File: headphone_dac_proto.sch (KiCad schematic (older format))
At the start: 66 parts, among them J1 USB_B_Mini, J2 Bluetooth, J3 Prog, J6 Headphones, U1 LT3042xMSE, U2 CY8C5888LTI-LP097, U3 CS4344, U4 TPA6139A2, Y1 Crystal_GND24

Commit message: ..
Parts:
- Y1: value Crystal_GND24 -> 12.288MHz
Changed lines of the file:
@@
 U 1 1 5F038FE4
 P 7200 9500
-F 0 "Y1" H 7006 9454 50  0000 R CNN
-F 1 "Crystal_GND24" H 7006 9545 50  0000 R CNN
+F 0 "Y1" H 7100 9300 50  0000 R CNN
+F 1 "12.288MHz" H 7750 9350 50  0000 R CNN
 F 2 "Crystal:Crystal_SMD_Abracon_ABM3B-4Pin_5.0x3.2mm" H 7200 9500 50  0001 C CNN
 F 3 "~" H 7200 9500 50  0001 C CNN

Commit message: Change programming connector. Finish BOM
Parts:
- removed J3: Prog, conn_prog:FTSH-105, symbol Connector_Generic:Conn_02x05_Odd_Even
- added J3: Conn_01x05_Male, Connector_PinHeader_2.54mm:PinHeader_1x05_P2.54mm_Vertical, symbol Connector:Conn_01x05_Male
- C1, C2, C27, C3, C32, C33, C34, C35, C36, C4: Manufacturer (none) -> KEMET; Manufacturer Part Number (none) -> C0603C105K3RAC7411; Mouser Part Number (none) -> 80-C0603C105K3RLR
- C10, C11, C12, C13, C14, C20, C22, C5, C6, C9: Manufacturer (none) -> KEMET; Manufacturer Part Number (none) -> C0603C104K5RAC3121; Mouser Part Number (none) -> 80-C603C104K5RAC3121
- C15, C16, C17, C21: Manufacturer (none) -> KEMET; Manufacturer Part Number (none) -> C0805C475K3RACTU; Mouser Part Number (none) -> 80-C0805C475K3RACTU
- C18, C19, C7, C8: Manufacturer (none) -> KEMET; Manufacturer Part Number (none) -> C0603C150K5RAC7867; Mouser Part Number (none) -> 80-C0603C150K5RACTU
- C23: Manufacturer (none) -> KEMET; Manufacturer Part Number (none) -> C0805C106K8RACAUTO; Mouser Part Number (none) -> 80-C0805C106K8RAUTO
- C24, C25, C26, C30, C31: Manufacturer (none) -> TDK; Manufacturer Part Number (none) -> CGA4J1X7R1E335K125AC; Mouser Part Number (none) -> 810-CGA4J1X7R1E335K
- C28, C29: Manufacturer (none) -> KEMET; Manufacturer Part Number (none) -> C0603C272J5GACAUTO; Mouser Part Number (none) -> 80-C0603C272J5GAUTO
- FB1: Manufacturer (none) -> TDK; Manufacturer Part Number (none) -> KMZ1608SHR601ATD25; Mouser Part Number (none) -> 810-KMZ1608SHR601ATD
- H1, H2, H3, H4, R1: Config (none) -> dnp
- J1: Manufacturer (none) -> Wurth Elektronik; Manufacturer Part Number (none) -> 65100516121; Mouser Part Number (none) -> 710-65100516121
- J2: Manufacturer (none) -> Harwin; Manufacturer Part Number (none) -> M20-9761046; Mouser Part Number (none) -> 855-M20-9761046
- J6: Manufacturer (none) -> CUI Devices; Manufacturer Part Number (none) -> SJ1-3535NG-GR; Mouser Part Number (none) -> 490-SJ1-3535NG-GR
- R10: Manufacturer (none) -> Vishay / Dale; Manufacturer Part Number (none) -> RCS060382K0FKEA; Mouser Part Number (none) -> 71-RCS060382K0FKEA
- R2, R3: Manufacturer (none) -> Vishay / Dale; Manufacturer Part Number (none) -> CRCW060327R0FKEAC; Mouser Part Number (none) -> 71-CRCW060327R0FKEAC
- R4: Manufacturer (none) -> Panasonic; Manufacturer Part Number (none) -> ERJ-UP3D1001V; Mouser Part Number (none) -> 667-ERJ-UP3D1001V
- R5: Manufacturer (none) -> Panasonic; Manufacturer Part Number (none) -> ERJ-PB3B3322V; Mouser Part Number (none) -> 667-ERJ-PB3B3322V
- R6, R7: Manufacturer (none) -> Panasonic; Manufacturer Part Number (none) -> ERJ-UP3F1002V; Mouser Part Number (none) -> 667-ERJ-UP3F1002V
- R8, R9: Manufacturer (none) -> Panasonic; Manufacturer Part Number (none) -> ERJ-UP3F4700V; Mouser Part Number (none) -> 667-ERJ-UP3F4700V
- RV1: Manufacturer (none) -> Bourns; Manufacturer Part Number (none) -> PTV09A-4025U-A104; Mouser Part Number (none) -> 652-PTV09A-4025UA104
- RV2, RV3: Manufacturer (none) -> Bourns; Manufacturer Part Number (none) -> PTV09A-4025F-B104; Mouser Part Number (none) -> 652-PTV09A4025FB104
- SW1, SW2, SW3: Manufacturer (none) -> ALPS; Manufacturer Part Number (none) -> SKHHDUA010; Mouser Part Number (none) -> 688-SKHHDU
- U1: Manufacturer (none) -> Analog Devices; Manufacturer Part Number (none) -> LT3042EMSE#PBF; Mouser Part Number (none) -> 584-LT3042EMSE#PBF
- U2: Mouser Part Number (none) -> 727-CY8C5888LTILP097
- U3: Manufacturer (none) -> Cirrus Logic; Manufacturer Part Number (none) -> CS4344-CZZR; Mouser Part Number (none) -> 777-CS4344-CZZR
- U4: Manufacturer (none) -> Texas Instruments; Manufacturer Part Number (none) -> TPA6139A2PWR; Mouser Part Number (none) -> 595-TPA6139A2PWR
- Y1: Manufacturer (none) -> ABRACON; Manufacturer Part Number (none) -> ABM3B-12.288MHZ-10-1-U-T; Mouser Part Number (none) -> 815-ABM3B-12.288-T
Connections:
- net labels added: swdck, swdio
- net labels removed: tck, tdi, tdo, tms
- wire segments 261 -> 250
- no-connect marks 48 -> 50

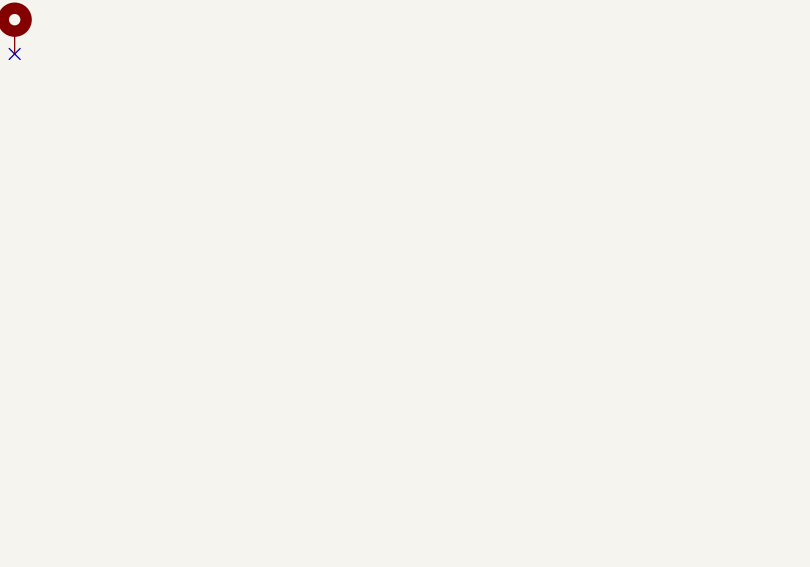
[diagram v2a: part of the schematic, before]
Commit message: Add logos and links. #networking
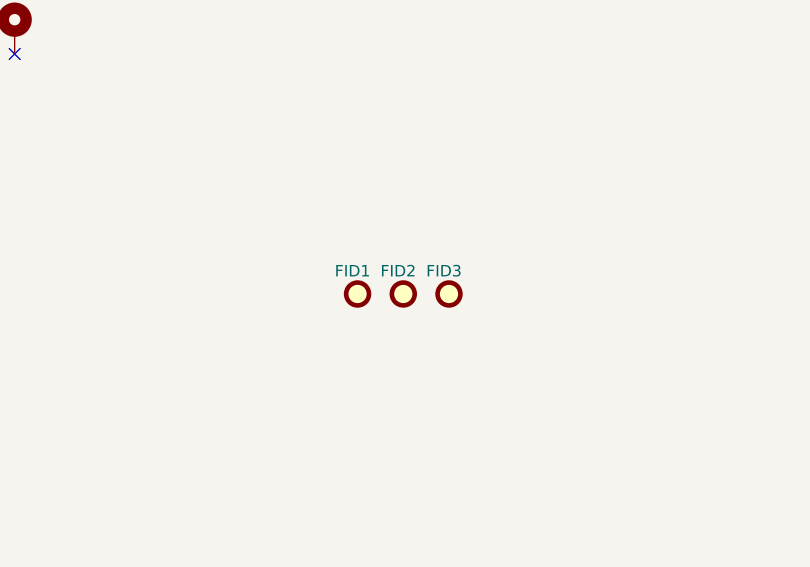
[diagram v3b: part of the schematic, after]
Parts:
- added FID1, FID2, FID3: ~, Fiducial:Fiducial_0.5mm_Mask1.5mm, symbol Mechanical:Fiducial
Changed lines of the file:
@@
 NoConn ~ 5450 7450
 NoConn ~ 5450 7550
+$Comp
+L Mechanical:Fiducial FID1
+U 1 1 5F164896
+P 12600 7700
+F 0 "FID1" H 12500 7800 50  0000 L CNN
+F 1 "~" H 12685 7655 50  0000 L CNN
+F 2 "Fiducial:Fiducial_0.5mm_Mask1.5mm" H 12600 7700 50  0001 C CNN
+F 3 "~" H 12600 7700 50  0001 C CNN
+F 4 "dnp" H 12600 7700 50  0001 C CNN "Config"
+	1    12600 7700
+	1    0    0    -1
+$EndComp
+$Comp
+L Mechanical:Fiducial FID2
+U 1 1 5F165556
+P 12800 7700
+F 0 "FID2" H 12700 7800 50  0000 L CNN
+F 1 "~" H 12885 7655 50  0000 L CNN
+F 2 "Fiducial:Fiducial_0.5mm_Mask1.5mm" H 12800 7700 50  0001 C CNN
+F 3 "~" H 12800 7700 50  0001 C CNN
+F 4 "dnp" H 12800 7700 50  0001 C CNN "Config"
+	1    12800 7700
+	1    0    0    -1
+$EndComp
+$Comp
+L Mechanical:Fiducial FID3
+U 1 1 5F1656BE
+P 13000 7700
+F 0 "FID3" H 12900 7800 50  0000 L CNN
+F 1 "~" H 13085 7655 50  0000 L CNN
+F 2 "Fiducial:Fiducial_0.5mm_Mask1.5mm" H 13000 7700 50  0001 C CNN
+F 3 "~" H 13000 7700 50  0001 C CNN
+F 4 "dnp" H 13000 7700 50  0001 C CNN "Config"
+	1    13000 7700
+	1    0    0    -1
+$EndComp
 $EndSCHEMATC

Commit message: Add 3dmodels to board
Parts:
- U2: symbol microcontroller_arm:CY8C5888LTI-LP097 -> headphone_dac_proto-rescue:CY8C5888LTI-LP097-microcontroller_arm
- U3: symbol audio_digital:CS4344 -> headphone_dac_proto-rescue:CS4344-audio_digital
- U4: symbol audio_amplifier:TPA6139A2 -> headphone_dac_proto-rescue:TPA6139A2-audio_amplifier
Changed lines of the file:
@@
 	5800 1650 6000 1650
 $Comp
-L audio_digital:CS4344 U3
+L headphone_dac_proto-rescue:CS4344-audio_digital U3
 U 1 1 5EFBA2D5
 P 9150 2200
@@
 $EndComp
 $Comp
-L microcontroller_arm:CY8C5888LTI-LP097 U2
+L headphone_dac_proto-rescue:CY8C5888LTI-LP097-microcontroller_arm U2
 U 1 1 5EEF718C
 P 6800 6950
@@
 Analog Inputs
 $Comp
-L audio_amplifier:TPA6139A2 U4
+L headphone_dac_proto-rescue:TPA6139A2-audio_amplifier U4
 U 1 1 5F8BD36E
 P 12650 2200

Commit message: Fix bom
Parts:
- R10: Manufacturer Vishay / Dale -> Yageo; Manufacturer Part Number RCS060382K0FKEA -> MFR-25FTE52-82K; Mouser Part Number 71-RCS060382K0FKEA -> 603-MFR-25FTE52-82K
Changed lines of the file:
@@
 F 2 "Resistor_THT:R_Axial_DIN0207_L6.3mm_D2.5mm_P15.24mm_Horizontal" V 11930 2750 50  0001 C CNN
 F 3 "~" H 12000 2750 50  0001 C CNN
-F 4 "Vishay / Dale" H 12000 2750 50  0001 C CNN "Manufacturer"
-F 5 "RCS060382K0FKEA" H 12000 2750 50  0001 C CNN "Manufacturer Part Number"
-F 6 "71-RCS060382K0FKEA" H 12000 2750 50  0001 C CNN "Mouser Part Number"
+F 4 "Yageo" H 12000 2750 50  0001 C CNN "Manufacturer"
+F 5 "MFR-25FTE52-82K" H 12000 2750 50  0001 C CNN "Manufacturer Part Number"
+F 6 "603-MFR-25FTE52-82K" H 12000 2750 50  0001 C CNN "Mouser Part Number"
 	1    12000 2750
 	1    0    0    -1
